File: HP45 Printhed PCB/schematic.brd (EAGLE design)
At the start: 35 x 55 mm, 38 parts, among them J1 87224-1, J10 640454-5, J2 87224-1, J3 87224-1, J4 87224-1, J5 87224-1, J6 87224-1, J7 87224-1, J8 87224-1, J9 87224-1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

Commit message: PCB
Completed board 1.0
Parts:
- added R11, R12: 1000Ω, resistor:R0603
- C1, C2, C3, C4, C5: device capacitor-wima:C2.5-3 -> rcl:C0603
- moved P1 44.5 mm to (2.51, 6.04)
- moved U11 35.5 mm to (8.01, 34.0), turned to 180 degrees
- moved C4 34.0 mm to (11.9, 50.6)
- moved U15 27.4 mm to (4.47, 36.5), turned to 180 degrees
- moved R6 27.0 mm to (14.1, 24.8), turned to 270 degrees
- moved R7 26.8 mm to (5.24, 17.3), turned to 270 degrees
- moved R3 26.8 mm to (5.33, 23.6), turned to 270 degrees
- moved C3 23.6 mm to (27.5, 25.3), turned to 90 degrees
- moved U18 23.0 mm to (1.82, 28.6), turned to 180 degrees
- moved C1 21.9 mm to (20.1, 36.2), turned to 180 degrees
- moved R1 20.8 mm to (20.2, 40.9), turned to 0 degrees
- moved PIC 19.4 mm to (12.5, 44.4)
- moved U14 18.8 mm to (1.71, 18.2), turned to 180 degrees
- moved R10 18.5 mm to (10.9, 11.2), turned to 90 degrees
- moved J1 17.9 mm to (7.94, 23.0)
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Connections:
- net PIC_MCLR renamed PICKIT_MCLR
- removed net PIC_VDD: C5.1, J10.2, PIC.17
- removed net VO: C2.1, Q1.2, R2.2
- new net N$12: PIC.10, PIC.12, PIC.13, PIC.14, PIC.15, PIC.23, R12.1
- new net N$3: PIC.18, PIC.3, PIC.4, PIC.6, PIC.7, R11.2
- new net PICKIT_VDD: C2.1, C5.1, J10.2, PIC.17, Q1.2, R2.2
- net GND: now also R11.1, R12.2, U2.11, U2.14, U3.11, U3.14
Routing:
- net PICKIT_VDD: track 0.00 -> 69.3 mm, vias 0 -> 2
- net SHIFTER_VCC_A: track 0.00 -> 51.9 mm, vias 0 -> 2
- net PIC_PGC: track 0.00 -> 48.1 mm, vias 0 -> 2
- net HEAD_P1: track 0.00 -> 45.9 mm
- net PIC_PGD: track 0.00 -> 44.2 mm, vias 0 -> 2
- net N$12: track 0.00 -> 40.5 mm, vias 0 -> 3
- net PICKIT_MCLR: track 0.00 -> 32.5 mm
- net N$11: track 0.00 -> 30.8 mm, vias 0 -> 1
- net HEAD_P2: track 0.00 -> 30.1 mm
- net +12V: track 0.00 -> 27.6 mm, vias 0 -> 12
- net N$3: track 0.00 -> 25.4 mm, vias 0 -> 3
- net HEAD_P4: track 0.00 -> 23.9 mm
- net N$9: track 0.00 -> 23.6 mm, vias 0 -> 2
- net HEAD_P3: track 0.00 -> 22.7 mm
- net GND: track 0.00 -> 20.2 mm, vias 0 -> 2
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- added copper zone on layer 16, net +12V
- added copper zone on layer 1, net GND

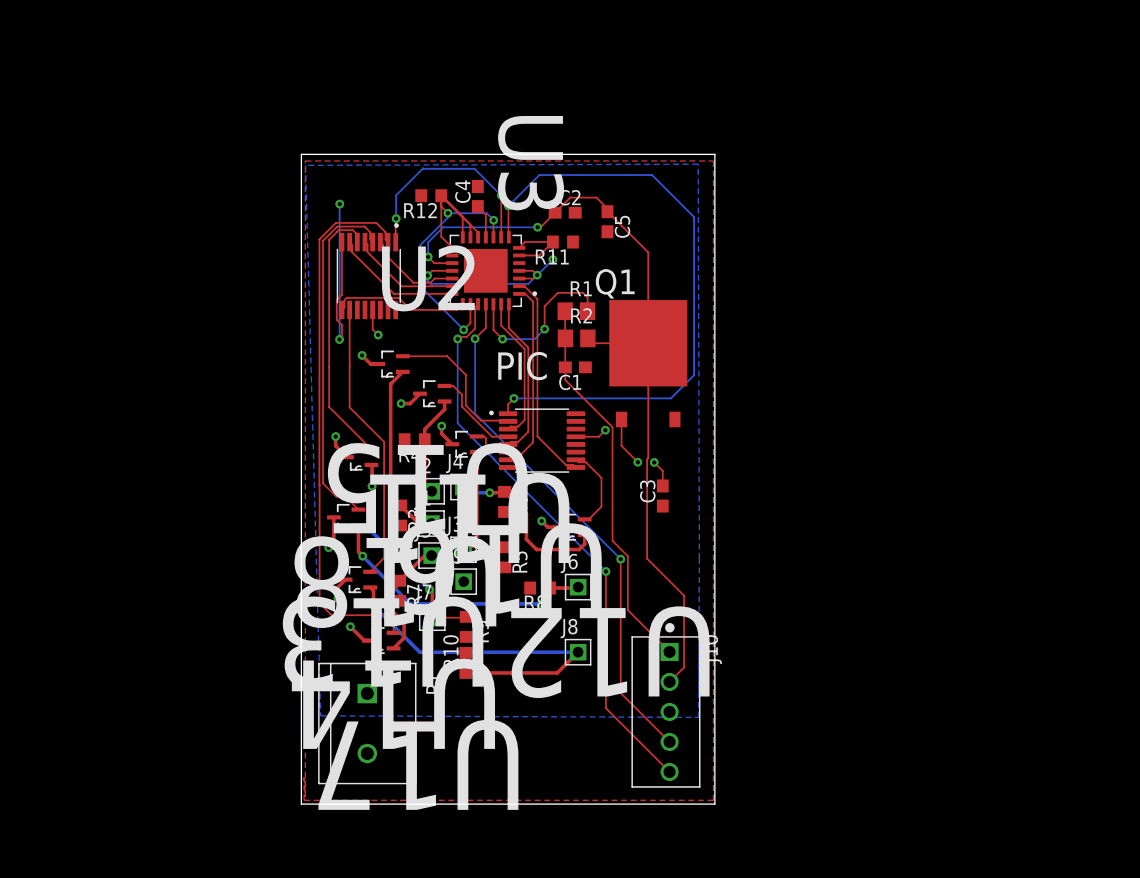
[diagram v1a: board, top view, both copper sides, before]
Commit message: PCB Changes
Revised pinheads, modified libraries
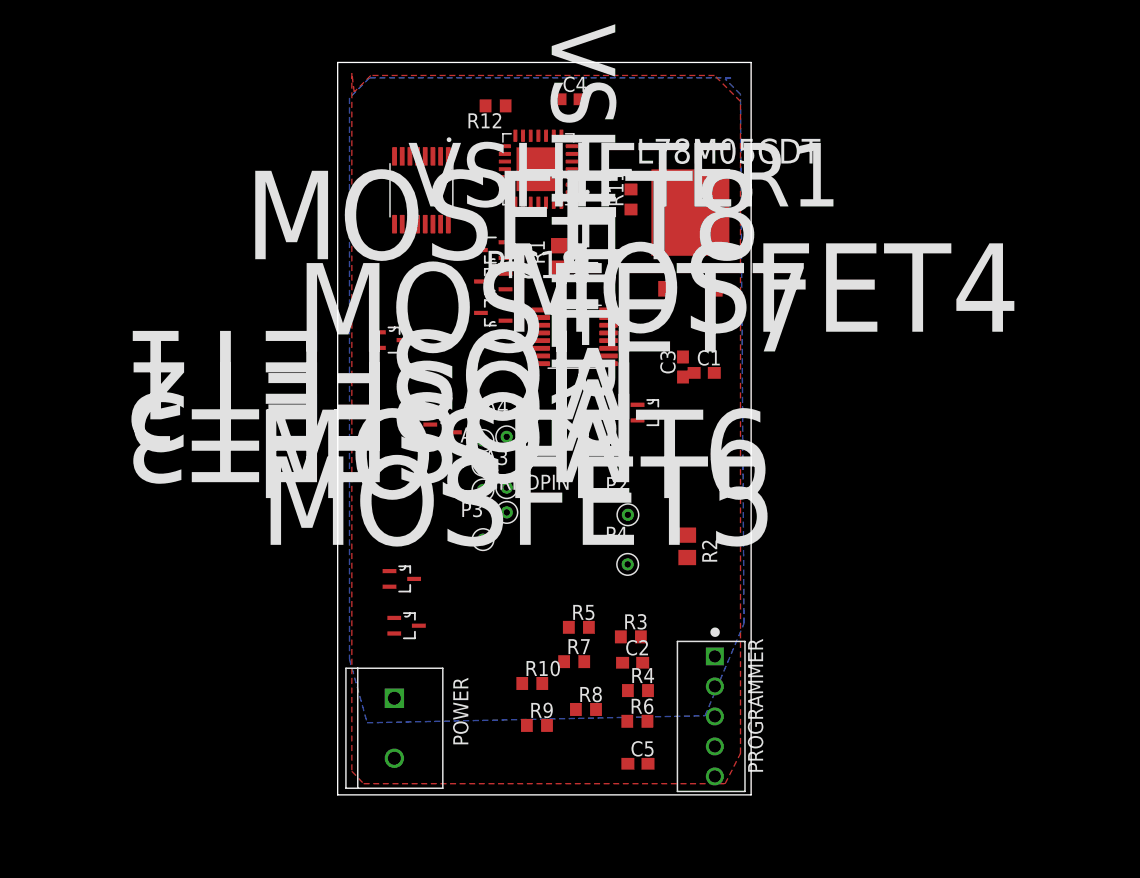
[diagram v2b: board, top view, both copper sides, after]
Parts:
- removed J1, J2, J3, J4, J5, J6, J7, J8, J9: 87224-1, 87224-1:HDRV1W68P0_1X1_213X213X1036
- removed J10: 640454-5, 640454-5:TE_640454-5
- removed PIC: PIC18F25K50T-I/ML, PIC18F25K50T-I_ML:QFN65P600X600X100-29N
- removed Q1: L78M05CDT, L78M05CDT:TO225P972X240-3N
- removed U11, U12, U13, U14, U15, U16, U17, U18: DMG1013UWQ-7, DMG1013UWQ-7:SOT65P210X110-3N
- removed U2, U3: CD4504BPWE4, CD4504BPWE4:SOP65P640X120-16N
- added A1, A2, A3, A4, GRNDPIN, P2, P3, P4: 0930, 0930:0930
- added L78M05CDT: L78M05CDT, L78M05CDT:TO225P972X240-3N
- added MOSFET1, MOSFET2, MOSFET3, MOSFET4, MOSFET5, MOSFET6, MOSFET7, MOSFET8: DMG1013UWQ-7, DMG1013UWQ-7:SOT65P210X110-3N
- added PIC18F: PIC18F25K50T-I/ML, PIC18F25K50T-I_ML:QFN65P600X600X100-29N
- added POWER: 282837-2, 282837-2:TE_282837-2
- added PROGRAMMER: 640454-5, 640454-5:TE_640454-5
- added VSHIFTER1, VSHIFTER2: CD4504BPWE4, CD4504BPWE4:SOP65P640X120-16N
- P1: value 282837-2 -> 0930; device 282837-2:TE_282837-2 -> 0930:0930
- moved C5 46.0 mm to (25.4, 2.63), turned to 0 degrees
- moved C2 38.5 mm to (25.0, 11.2)
- moved R4 28.4 mm to (25.4, 8.83), turned to 0 degrees
- moved P1 22.1 mm to (12.3, 25.8), turned to 0 degrees
- moved R3 22.0 mm to (24.8, 13.4), turned to 0 degrees
- moved R6 21.7 mm to (25.4, 6.23), turned to 0 degrees
- moved R2 19.9 mm to (29.6, 21.0), turned to 270 degrees
- moved R7 16.0 mm to (20.0, 11.3), turned to 0 degrees
- moved C4 11.3 mm to (19.7, 58.9), turned to 0 degrees
- moved C3 11.1 mm to (29.2, 36.2)
- moved R8 11.0 mm to (21.0, 7.23), turned to 0 degrees
- moved C1 10.9 mm to (31.0, 35.7), turned to 0 degrees
- moved R9 10.3 mm to (16.9, 5.88), turned to 0 degrees
- moved R12 9.36 mm to (13.4, 58.3)
- moved R5 8.63 mm to (20.4, 14.2), turned to 0 degrees
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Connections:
- net +12V: now also L78M05CDT.1, MOSFET1.2, MOSFET2.2, MOSFET3.2, MOSFET4.2, MOSFET5.2, MOSFET6.2, MOSFET7.2, MOSFET8.2, POWER.1, VSHIFTER1.16, VSHIFTER2.16; no longer P1.1, Q1.1, U11.3, U12.3, U13.3, U14.3, U15.3, U16.3, U17.3, U18.3, U2.13, U3.13
- net CTRL_A1: now also PIC18F.27, VSHIFTER1.3; no longer PIC.27, U2.3
- net CTRL_A2: now also PIC18F.28, VSHIFTER1.5; no longer PIC.28, U2.5
- net CTRL_A3: now also PIC18F.1, VSHIFTER1.7; no longer PIC.1, U2.7
- net CTRL_A4: now also PIC18F.2, VSHIFTER1.9; no longer PIC.2, U2.9
- net CTRL_P1: now also PIC18F.19, VSHIFTER2.3; no longer PIC.19, U3.3
- net CTRL_P2: now also PIC18F.20, VSHIFTER2.5; no longer PIC.20, U3.5
- net CTRL_P3: now also PIC18F.21, VSHIFTER2.7; no longer PIC.21, U3.7
- net CTRL_P4: now also PIC18F.22, VSHIFTER2.9; no longer PIC.22, U3.9
- net GND: now also GRNDPIN.1, L78M05CDT.2, PIC18F.16, PIC18F.5, POWER.2, PROGRAMMER.3, VSHIFTER1.11, VSHIFTER1.14, VSHIFTER1.8, VSHIFTER2.11, VSHIFTER2.14, VSHIFTER2.8; no longer J10.3, J9.1, P1.2, PIC.16, PIC.5, Q1.3, U2.11, U2.14, U2.8, U3.11, U3.14, U3.8
- net HEAD_A1: now also MOSFET1.1, VSHIFTER1.2; no longer U15.2, U2.2
- net HEAD_A2: now also MOSFET2.1, VSHIFTER1.4; no longer U11.2, U2.4
- net HEAD_A3: now also MOSFET3.1, VSHIFTER1.6; no longer U16.2, U2.6
- net HEAD_A4: now also MOSFET4.1, VSHIFTER1.10; no longer U12.2, U2.10
- net HEAD_P1: now also MOSFET5.1, VSHIFTER2.2; no longer U17.2, U3.2
- net HEAD_P2: now also MOSFET6.1, VSHIFTER2.4; no longer U13.2, U3.4
- net HEAD_P3: now also MOSFET7.1, VSHIFTER2.6; no longer U18.2, U3.6
- net HEAD_P4: now also MOSFET8.1, VSHIFTER2.10; no longer U14.2, U3.10
- net N$1: now also PIC18F.11; no longer PIC.11
- net N$10: now also MOSFET7.3, P3.1; no longer J7.1, U18.1
- net N$11: now also MOSFET8.3, P4.1; no longer J8.1, U14.1
- net N$12: now also PIC18F.10, PIC18F.12, PIC18F.13, PIC18F.14, PIC18F.15, PIC18F.23; no longer PIC.10, PIC.12, PIC.13, PIC.14, PIC.15, PIC.23
- net N$2: now also A1.1, MOSFET1.3; no longer J1.1, U15.1
- net N$3: now also PIC18F.18, PIC18F.3, PIC18F.4, PIC18F.6, PIC18F.7; no longer PIC.18, PIC.3, PIC.4, PIC.6, PIC.7
- net N$4: now also A2.1, MOSFET2.3; no longer J2.1, U11.1
- net N$5: now also A3.1, MOSFET3.3; no longer J3.1, U16.1
- net N$6: now also PIC18F.26; no longer PIC.26
- net N$7: now also A4.1, MOSFET4.3; no longer J4.1, U12.1
- net N$8: now also MOSFET5.3, P1.1; no longer J5.1, U17.1
- net N$9: now also MOSFET6.3, P2.1; no longer J6.1, U13.1
- net PICKIT_MCLR: now also PROGRAMMER.1; no longer J10.1
- net PICKIT_VDD: now also PIC18F.17, PROGRAMMER.2; no longer J10.2, PIC.17, Q1.2
- net PIC_PGC: now also PIC18F.24, PROGRAMMER.5; no longer J10.5, PIC.24
- net PIC_PGD: now also PIC18F.25, PROGRAMMER.4; no longer J10.4, PIC.25
- net SHIFTER_VCC_A: now also PIC18F.8, VSHIFTER1.1; no longer PIC.8, U2.1
- net SHIFTER_VCC_P: now also PIC18F.9, VSHIFTER2.1; no longer PIC.9, U3.1
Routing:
- net PICKIT_VDD: track 69.3 -> 0.00 mm, vias 2 -> 0
- net SHIFTER_VCC_A: track 51.9 -> 0.00 mm, vias 2 -> 0
- net PIC_PGC: track 48.1 -> 0.00 mm, vias 2 -> 0
- net HEAD_P1: track 45.9 -> 0.00 mm
- net PIC_PGD: track 44.2 -> 0.00 mm, vias 2 -> 0
- net N$12: track 40.5 -> 0.00 mm, vias 3 -> 0
- net PICKIT_MCLR: track 32.5 -> 0.00 mm
- net N$11: track 30.8 -> 0.00 mm, vias 1 -> 0
- net HEAD_P2: track 30.1 -> 0.00 mm
- net +12V: track 27.6 -> 0.00 mm, vias 12 -> 0
- net N$3: track 25.4 -> 0.00 mm, vias 3 -> 0
- net HEAD_P4: track 23.9 -> 0.00 mm
- net N$9: track 23.6 -> 0.00 mm, vias 2 -> 0
- net HEAD_P3: track 22.7 -> 0.00 mm
- net GND: track 20.2 -> 0.00 mm, vias 2 -> 0
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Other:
- board size 35 x 55 mm -> 35 x 62 mm

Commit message: PCB
Done
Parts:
- moved C5 58.3 mm to (10.1, 58.9), turned to 180 degrees
- moved R4 28.0 mm to (12.8, 33.8)
- moved C2 27.6 mm to (31.9, 37.9), turned to 270 degrees
- moved R2 26.6 mm to (23.6, 47.0), turned to 0 degrees
- moved R6 23.5 mm to (17.5, 28.4), turned to 270 degrees
- moved R3 21.3 mm to (9.28, 28.0), turned to 270 degrees
- moved MOSFET6 18.3 mm to (4.53, 36.6)
- moved R8 15.7 mm to (21.8, 22.9), turned to 270 degrees
- moved R7 15.1 mm to (8.98, 21.6), turned to 270 degrees
- moved R9 13.4 mm to (13.2, 18.8)
- moved R5 11.8 mm to (18.0, 25.8)
- moved MOSFET8 11.1 mm to (5.26, 27.4)
- moved C1 11.1 mm to (23.9, 44.2)
- moved R10 10.7 mm to (21.9, 18.6), turned to 270 degrees
- moved MOSFET7 10.5 mm to (5.50, 40.6)
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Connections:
- net PICKIT_VDD: now also L78M05CDT.3
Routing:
- net PICKIT_VDD: track 0.00 -> 76.8 mm
- net PIC_PGC: track 0.00 -> 54.3 mm, vias 0 -> 1
- net PIC_PGD: track 0.00 -> 49.9 mm, vias 0 -> 1
- net HEAD_P1: track 0.00 -> 49.3 mm
- net PICKIT_MCLR: track 0.00 -> 41.7 mm
- net N$9: track 0.00 -> 36.9 mm, vias 0 -> 1
- net N$11: track 0.00 -> 32.7 mm, vias 0 -> 1
- net HEAD_P2: track 0.00 -> 24.9 mm
- net N$10: track 0.00 -> 24.3 mm, vias 0 -> 1
- net +12V: track 0.00 -> 24.1 mm, vias 0 -> 11
- net HEAD_P4: track 0.00 -> 23.1 mm
- net N$2: track 0.00 -> 21.6 mm
- net N$3: track 0.00 -> 21.0 mm, vias 0 -> 2
- net SHIFTER_VCC_A: track 0.00 -> 20.7 mm, vias 0 -> 2
- net HEAD_P3: track 0.00 -> 19.0 mm
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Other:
- board size 35 x 62 mm -> 35.1 x 59.9 mm

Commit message: Done NOw?
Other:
- board size 35.1 x 59.9 mm -> 35.6 x 59.9 mm

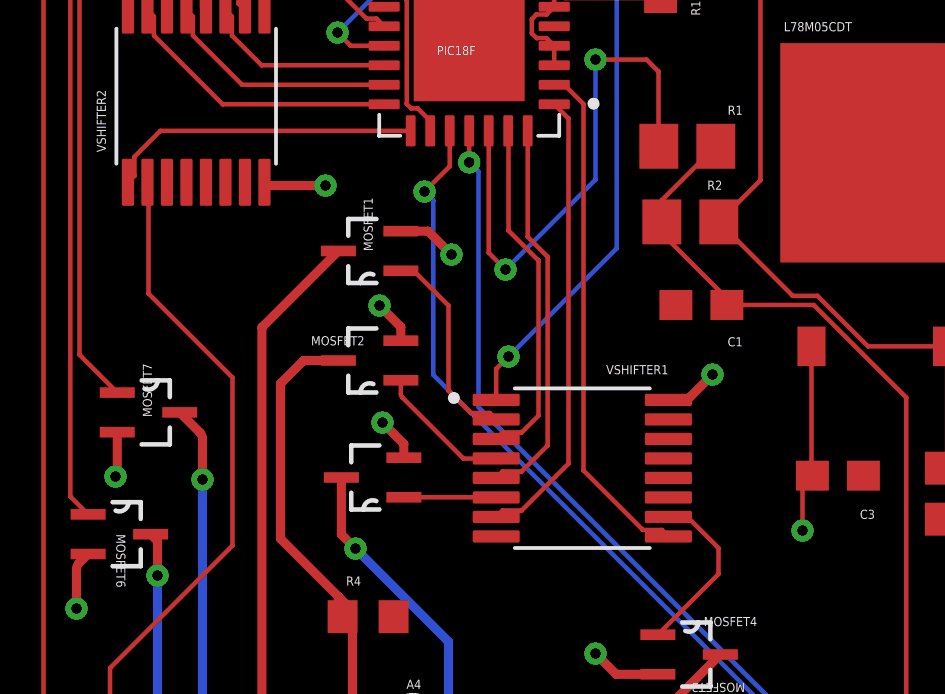
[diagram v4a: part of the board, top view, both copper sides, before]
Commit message: Minor FIx
PCB - added Select pin from Shifter to Low Logic with 10Ω Resistor intermeditate
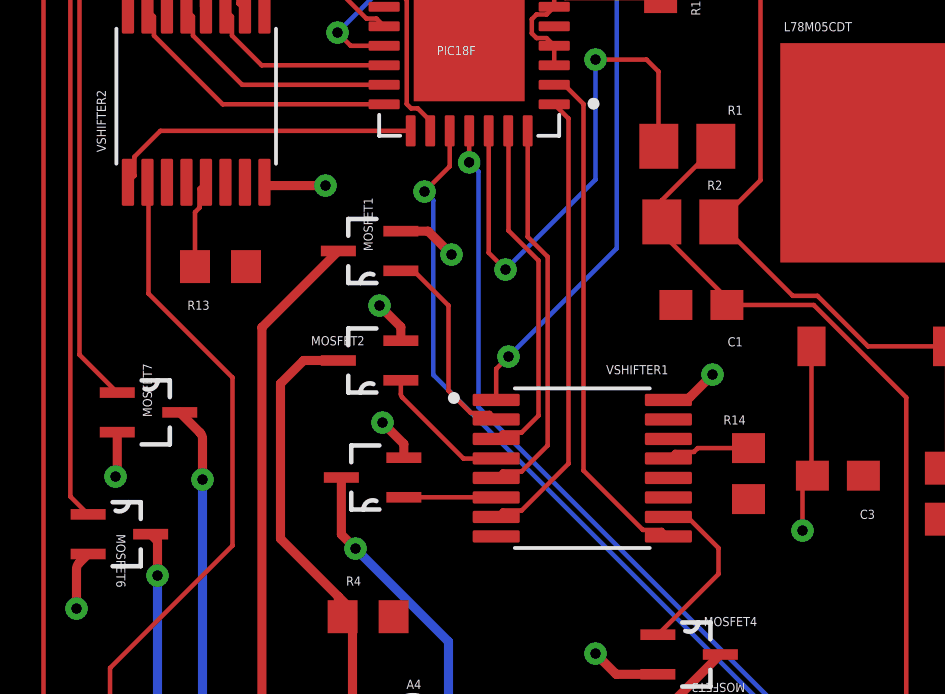
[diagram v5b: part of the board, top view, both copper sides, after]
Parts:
- added R13, R14: 10Ω, rcl:R0603
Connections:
- new net N$13: R14.2, VSHIFTER1.13
- new net N$14: R13.2, VSHIFTER2.13
- net GND: now also R13.1, R14.1
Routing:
- net N$14: track 0.00 -> 2.96 mm
- net N$13: track 0.00 -> 2.81 mm
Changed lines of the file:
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@@
 <attribute name="PRICE" value="0.26 USD" x="7.09" y="51.18" size="1.778" layer="27" rot="R270" display="off"/>
+</element>
+<element name="R13" library="rcl" library_urn="urn:adsk.eagle:library:334" package="R0603" package3d_urn="urn:adsk.eagle:package:23555/2" value="10Ω" x="7.9" y="45.5" smashed="yes" rot="R180">
+<attribute name="NAME" x="7.535" y="44.365" size="0.3048" layer="25" rot="R180"/>
+<attribute name="SPICEPREFIX" value="R" x="7.9" y="45.5" size="1.778" layer="27" rot="R180" display="off"/>
+<attribute name="VALUE" x="8.535" y="47.405" size="1.27" layer="27" rot="R180"/>
+</element>
+<element name="R14" library="rcl" library_urn="urn:adsk.eagle:library:334" package="R0603" package3d_urn="urn:adsk.eagle:package:23555/2" value="10Ω" x="25.5" y="38.6" smashed="yes" rot="R90">
+<attribute name="NAME" x="24.665" y="40.235" size="0.3048" layer="25"/>
+<attribute name="SPICEPREFIX" value="R" x="25.5" y="38.6" size="1.778" layer="27" rot="R90" display="off"/>
+<attribute name="VALUE" x="27.405" y="37.965" size="1.27" layer="27" rot="R90"/>
 </element>
 </elements>
@@
 </polygon>
 <contactref element="L78M05CDT" pad="2"/>
+<contactref element="R14" pad="1"/>
+<contactref element="R13" pad="1"/>
 <wire x1="15.38" y1="58.87" x2="13.355" y2="54.16" width="0" layer="19" extent="1-1"/>
 <wire x1="31.88" y1="37.08" x2="29.33" y2="38.53" width="0" layer="19" extent="1-1"/>
@@
 <wire x1="6.212125" y1="22.212125" x2="5.1" y2="21.1" width="0.3048" layer="1"/>
 </signal>
+<signal name="N$13">
+<contactref element="R14" pad="2"/>
+<contactref element="VSHIFTER1" pad="13"/>
+<wire x1="25.5" y1="39.45" x2="23.80826875" y2="39.45" width="0.1524" layer="1"/>
+<wire x1="23.80826875" y1="39.45" x2="23.67966875" y2="39.3214" width="0.1524" layer="1"/>
+<wire x1="23.67966875" y1="39.3214" x2="23.0464" y2="39.3214" width="0.1524" layer="1"/>
+<wire x1="23.0464" y1="39.3214" x2="22.83" y2="39.105" width="0.1524" layer="1"/>
+</signal>
+<signal name="N$14">
+<contactref element="R13" pad="2"/>
+<contactref element="VSHIFTER2" pad="13"/>
+<wire x1="7.05" y1="45.5" x2="7.05" y2="47.31173125" width="0.1524" layer="1"/>
+<wire x1="7.05" y1="47.31173125" x2="7.1986" y2="47.46033125" width="0.1524" layer="1"/>
+<wire x1="7.1986" y1="47.46033125" x2="7.1986" y2="48.0936" width="0.1524" layer="1"/>
+<wire x1="7.1986" y1="48.0936" x2="7.415" y2="48.31" width="0.1524" layer="1"/>
+</signal>
 </signals>
